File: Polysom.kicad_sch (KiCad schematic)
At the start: 0 parts

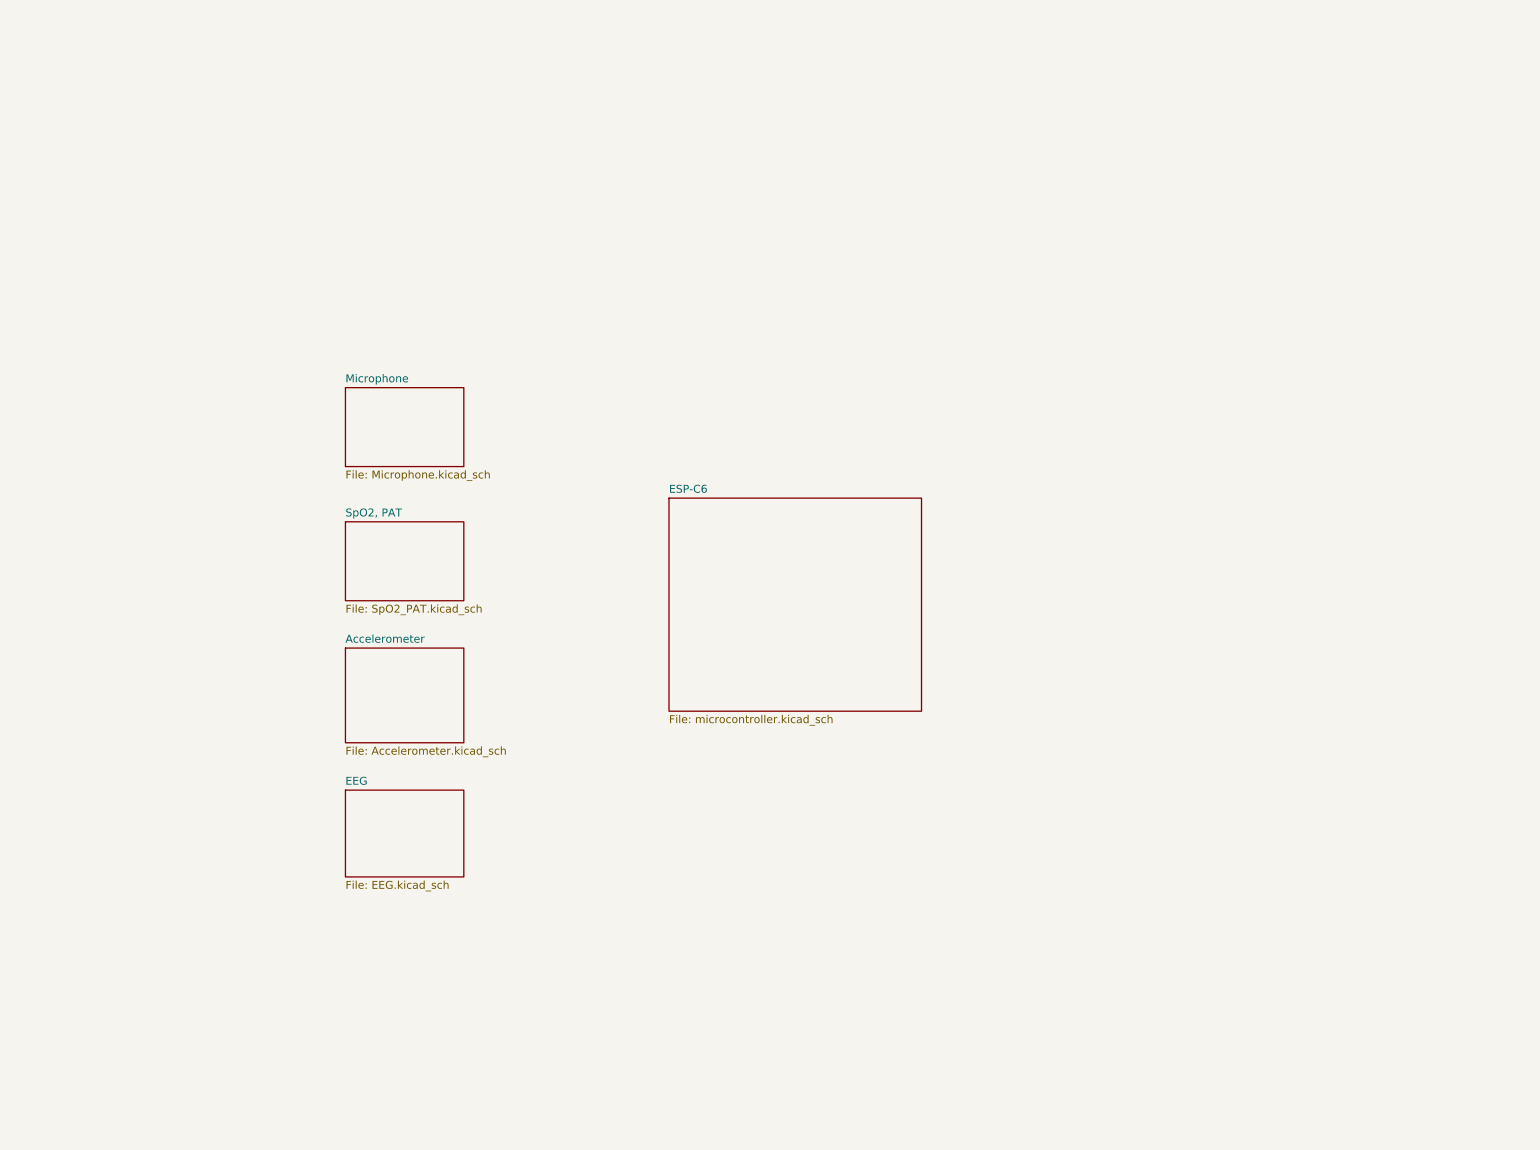
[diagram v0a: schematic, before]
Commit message: top-level structure and ESP32-C6 pin assignments nearly sorted
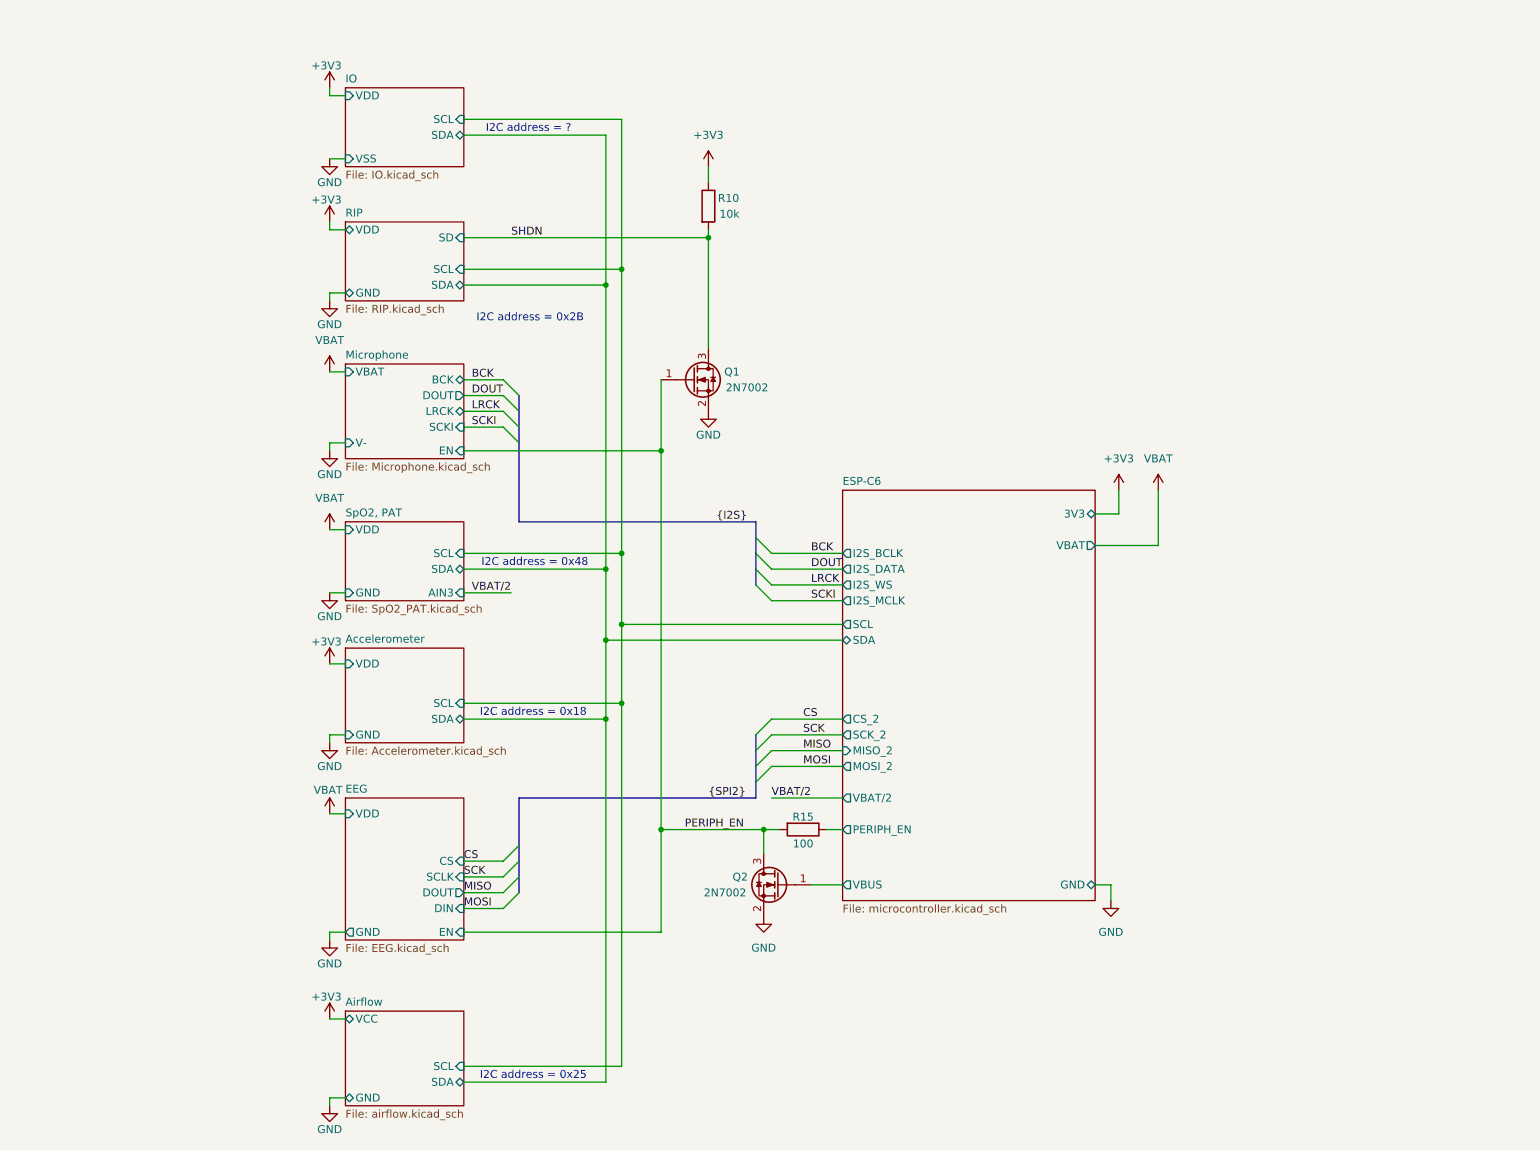
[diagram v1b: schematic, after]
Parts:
- added Q1, Q2: 2N7002, Package_TO_SOT_SMD:SOT-23, symbol Transistor_FET:2N7002
- added R10: 10k, Resistor_SMD:R_0603_1608Metric, symbol Device:R
- added R15: 100, Resistor_SMD:R_0603_1608Metric, symbol Device:R
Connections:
- new net +3V3: R10.1
- new net ESP-C6/PERIPH_EN: R15.1
- new net ESP-C6/VBUS: Q2.1 (G)
- new net GND: Q1.2 (S), Q2.2 (S)
- new net PERIPH_EN: Q1.1 (G), Q2.3 (D), R15.2
- new net SHDN: Q1.3 (D), R10.2
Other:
- added sheet Airflow (airflow.kicad_sch)
- added sheet IO (IO.kicad_sch)
- added sheet RIP (RIP.kicad_sch)
- sheet Accelerometer ports: added GND, SCL, SDA, VDD; removed none
- sheet EEG ports: added CS, DIN, DOUT, EN, GND, SCLK, VDD; removed none
- sheet ESP-C6 ports: added 3V3, CS_2, GND, I2S_BCLK, I2S_DATA, I2S_MCLK, I2S_WS, MISO_2, MOSI_2, PERIPH_EN, SCK_2, SCL, SDA, VBAT, VBAT/2, VBUS; removed none
- sheet Microphone ports: added BCK, DOUT, EN, LRCK, SCKI, V-, VBAT; removed none
- sheet SpO2, PAT ports: added AIN3, GND, SCL, SDA, VDD; removed none
- note added: "I2C address = 0x18"
- note added: "I2C address = 0x25"
- note added: "I2C address = 0x2B"
- note added: "I2C address = 0x48"
- note added: "I2C address = ?"
- company: (none) -> Sunrise designs
- title: (none) -> Open polysomnography board

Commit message: text comments sections added
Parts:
- added FB1, FB2: FerriteBead, Inductor_SMD:L_0603_1608Metric, symbol Device:FerriteBead
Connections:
- net +3V3: now also FB1.1
- net VBAT: now also FB2.1
- new net ESP-C6/3V3: FB1.2
- new net ESP-C6/VBAT: FB2.2
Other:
- note added: "Ipsum lorem"
- note added: "What's going on here:"
- moved on the sheet: Q1, Q2, R10, R15

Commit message: some work on sch and docs added
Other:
- sheet ESP-C6 ports: added {I2S}; removed I2S_DATA, I2S_MCLK, I2S_WS
- sheet Microphone ports: added none; removed BCK, DOUT, LRCK, SCKI
